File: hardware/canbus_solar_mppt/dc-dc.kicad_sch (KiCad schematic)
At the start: 58 parts

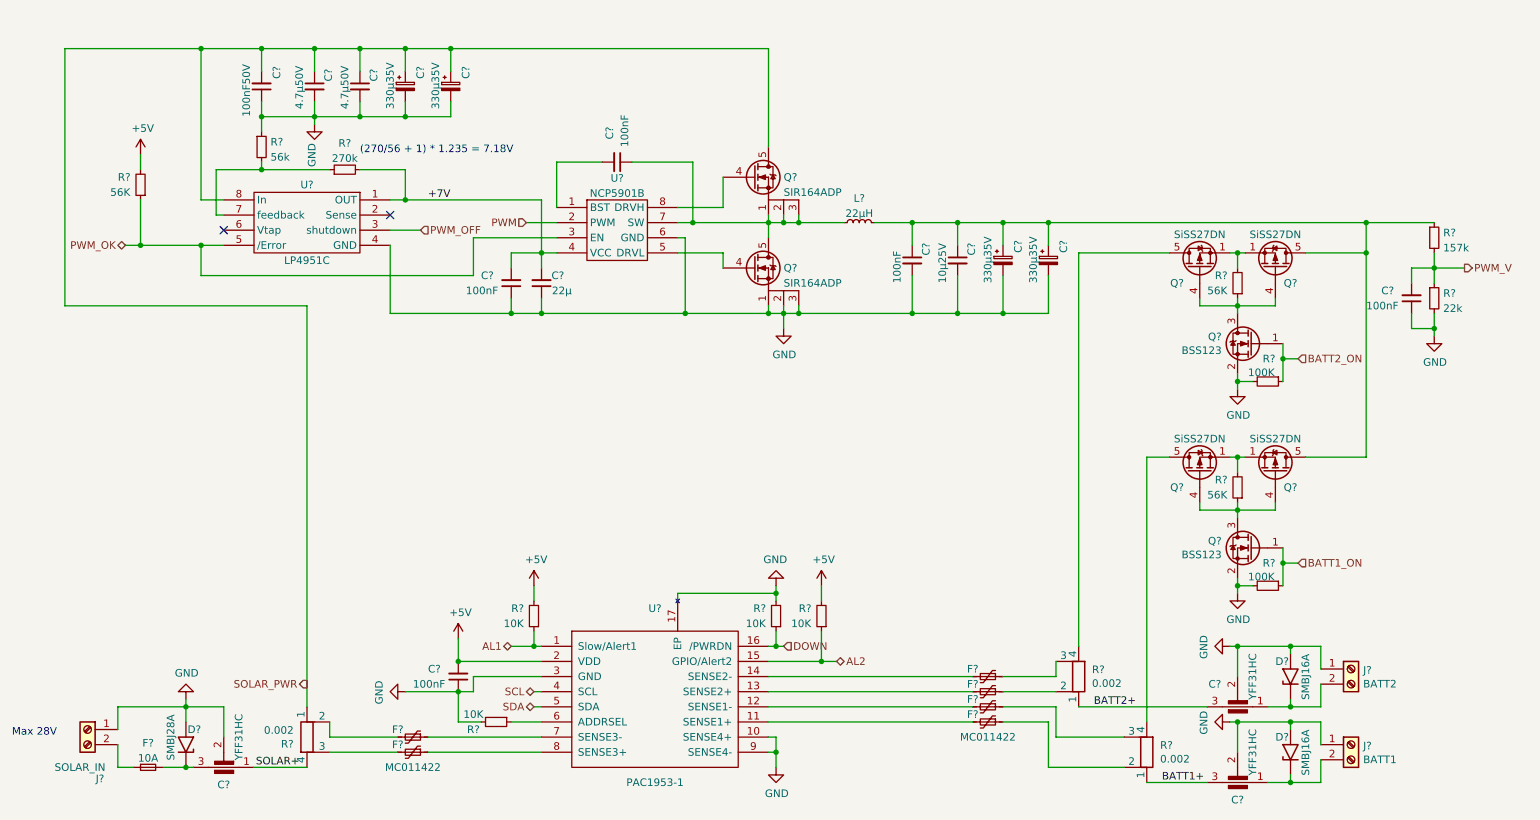
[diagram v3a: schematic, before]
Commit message: Add more signals between pic18 and DC/DC
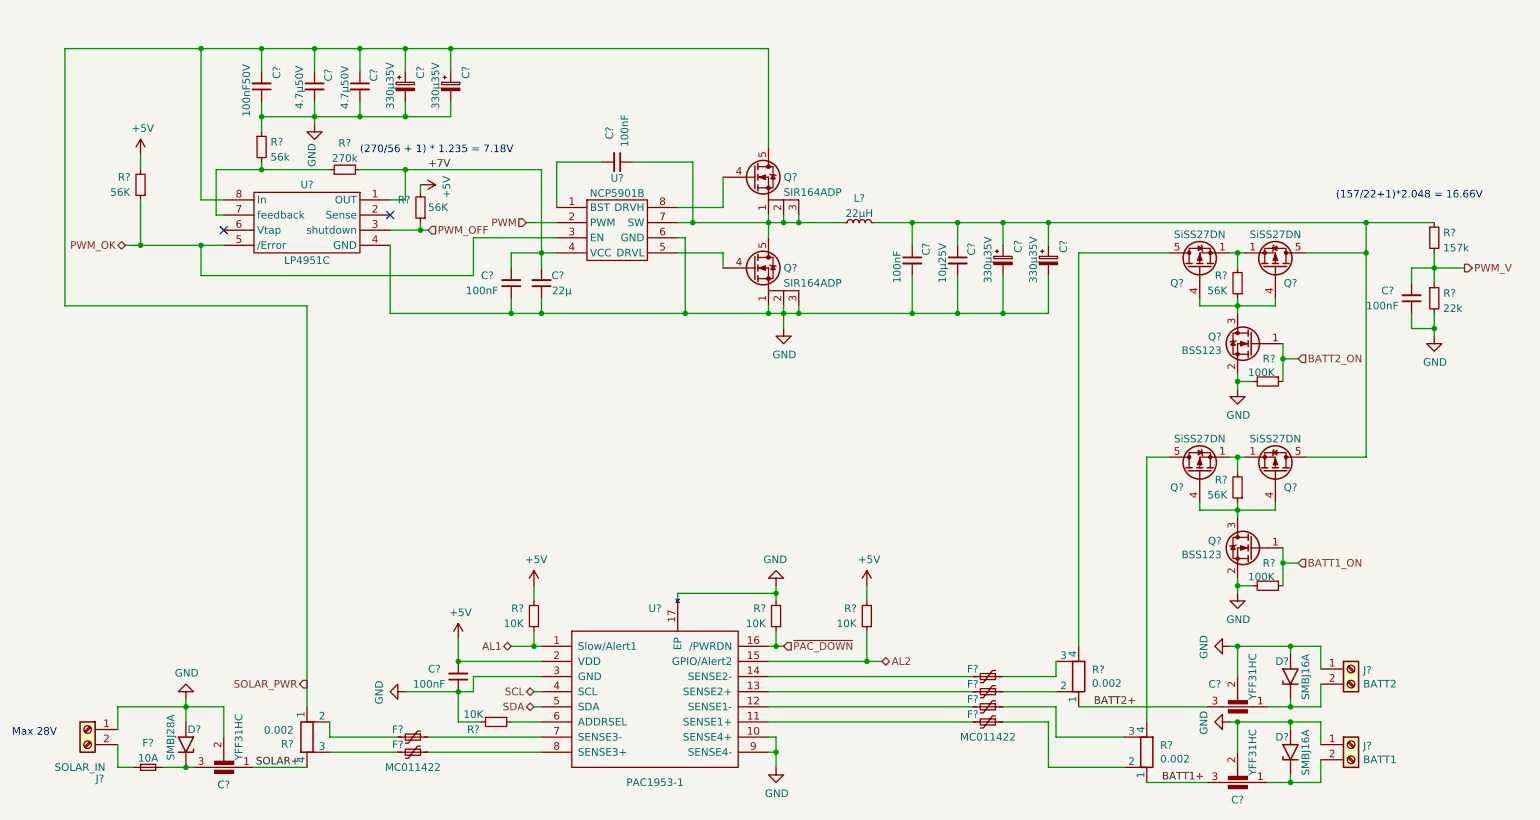
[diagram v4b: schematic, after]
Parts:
- added R?: 56K, Resistor_THT:R_Axial_DIN0207_L6.3mm_D2.5mm_P7.62mm_Horizontal, symbol Device:R_Small
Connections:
- net +5V: now also R?.2
- net PWM_OFF: now also R?.1
- net DOWN renamed ~{PAC_DOWN}
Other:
- note added: "(157/22+1)*2.048 = 16.66V"
- moved on the sheet: R?
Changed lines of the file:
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@@
   (junction (at 204.47 58.42) (diameter 0) (color 0 0 0 0)
   )
+  (junction (at 99.06 59.69) (diameter 0) (color 0 0 0 0)
+  )
   (junction (at 119.38 63.5) (diameter 0) (color 0 0 0 0)
   )
-  (junction (at 96.52 54.61) (diameter 0) (color 0 0 0 0)
-  )
   (junction (at 72.39 40.64) (diameter 0) (color 0 0 0 0)
   )
@@
   (junction (at 52.07 62.23) (diameter 0) (color 0 0 0 0)
   )
+  (junction (at 96.52 49.53) (diameter 0) (color 0 0 0 0)
+  )
   (junction (at 257.81 63.5) (diameter 0) (color 0 0 0 0)
   )
@@
   (junction (at 62.23 62.23) (diameter 0) (color 0 0 0 0)
   )
-  (junction (at 166.37 132.08) (diameter 0) (color 0 0 0 0)
+  (junction (at 173.99 132.08) (diameter 0) (color 0 0 0 0)
   )
   (junction (at 181.61 73.66) (diameter 0) (color 0 0 0 0)
@@
     (stroke (width 0) (type default) (color 0 0 0 0))
   )
+  (wire (pts (xy 119.38 49.53) (xy 119.38 63.5))
+    (stroke (width 0) (type default) (color 0 0 0 0))
+  )
   (wire (pts (xy 62.23 29.21) (xy 62.23 54.61))
     (stroke (width 0) (type default) (color 0 0 0 0))
@@
     (stroke (width 0) (type default) (color 0 0 0 0))
   )
-  (wire (pts (xy 157.48 132.08) (xy 166.37 132.08))
+  (wire (pts (xy 157.48 132.08) (xy 173.99 132.08))
     (stroke (width 0) (type default) (color 0 0 0 0))
   )
@@
     (stroke (width 0) (type default) (color 0 0 0 0))
   )
-  (wire (pts (xy 119.38 54.61) (xy 119.38 63.5))
-    (stroke (width 0) (type default) (color 0 0 0 0))
-  )
   (wire (pts (xy 96.52 40.64) (xy 104.14 40.64))
     (stroke (width 0) (type default) (color 0 0 0 0))
   )
+  (wire (pts (xy 99.06 52.07) (xy 99.06 53.34))
+    (stroke (width 0) (type default) (color 0 0 0 0))
+  )
   (wire (pts (xy 142.24 55.88) (xy 149.86 55.88))
     (stroke (width 0) (type default) (color 0 0 0 0))
@@
     (stroke (width 0) (type default) (color 0 0 0 0))
   )
-  (wire (pts (xy 166.37 132.08) (xy 166.37 127))
+  (wire (pts (xy 173.99 132.08) (xy 173.99 127))
     (stroke (width 0) (type default) (color 0 0 0 0))
   )
@@
     (stroke (width 0) (type default) (color 0 0 0 0))
   )
-  (wire (pts (xy 166.37 132.08) (xy 168.91 132.08))
+  (wire (pts (xy 173.99 132.08) (xy 176.53 132.08))
     (stroke (width 0) (type default) (color 0 0 0 0))
   )
@@
     (stroke (width 0) (type default) (color 0 0 0 0))
   )
+  (wire (pts (xy 96.52 49.53) (xy 119.38 49.53))
+    (stroke (width 0) (type default) (color 0 0 0 0))
+  )
   (wire (pts (xy 234.95 97.79) (xy 236.22 97.79))
     (stroke (width 0) (type default) (color 0 0 0 0))
@@
     (stroke (width 0) (type default) (color 0 0 0 0))
   )
-  (wire (pts (xy 96.52 54.61) (xy 119.38 54.61))
-    (stroke (width 0) (type default) (color 0 0 0 0))
-  )
   (wire (pts (xy 269.24 66.04) (xy 269.24 68.58))
     (stroke (width 0) (type default) (color 0 0 0 0))
@@
     (stroke (width 0) (type default) (color 0 0 0 0))
   )
+  (wire (pts (xy 99.06 58.42) (xy 99.06 59.69))
+    (stroke (width 0) (type default) (color 0 0 0 0))
+  )
   (wire (pts (xy 114.3 71.12) (xy 114.3 73.66))
     (stroke (width 0) (type default) (color 0 0 0 0))
@@
     (stroke (width 0) (type default) (color 0 0 0 0))
   )
-  (wire (pts (xy 166.37 121.92) (xy 166.37 119.38))
+  (wire (pts (xy 173.99 121.92) (xy 173.99 119.38))
     (stroke (width 0) (type default) (color 0 0 0 0))
   )
@@
   )
   (wire (pts (xy 236.22 97.79) (xy 236.22 100.33))
+    (stroke (width 0) (type default) (color 0 0 0 0))
+  )
+  (wire (pts (xy 99.06 59.69) (xy 100.33 59.69))
     (stroke (width 0) (type default) (color 0 0 0 0))
   )
@@
     (effects (font (size 1.27 1.27)) (justify left bottom))
   )
+  (text "(157/22+1)*2.048 = 16.66V" (at 252.73 54.61 0)
+    (effects (font (size 1.27 1.27)) (justify left bottom))
+  )
   (text "(270/56 + 1) * 1.235 = 7.18V" (at 88.9 46.99 0)
     (effects (font (size 1.27 1.27)) (justify left bottom))
   )
-  (label "+7V" (at 100.33 54.61 0)
+  (label "+7V" (at 100.33 49.53 0)
     (effects (font (size 1.27 1.27)) (justify left bottom))
   )
@@
     (effects (font (size 1.27 1.27)) (justify right))
   )
-  (hierarchical_label "PWM_OFF" (shape input) (at 99.06 59.69 0)
+  (hierarchical_label "PWM_OFF" (shape input) (at 100.33 59.69 0)
     (effects (font (size 1.27 1.27)) (justify left))
   )
@@
     (effects (font (size 1.27 1.27)) (justify right))
   )
-  (hierarchical_label "AL2" (shape bidirectional) (at 168.91 132.08 0)
+  (hierarchical_label "AL2" (shape bidirectional) (at 176.53 132.08 0)
     (effects (font (size 1.27 1.27)) (justify left))
   )
@@
     (effects (font (size 1.27 1.27)) (justify right))
   )
-  (hierarchical_label "DOWN" (shape input) (at 160.02 129.54 0)
+  (hierarchical_label "~{PAC_DOWN}" (shape input) (at 160.02 129.54 0)
     (effects (font (size 1.27 1.27)) (justify left))
   )
@@
     (pin "1")
     (pin "2")
+  )
+  (symbol (lib_id "power:+5V") (at 99.06 52.07 270) (unit 1)
+    (in_bom yes) (on_board yes)
+    (property "Reference" "#PWR?" (id 0) (at 95.25 52.07 0)
+      (effects (font (size 1.27 1.27)) hide)
+    )
+    (property "Value" "+5V" (id 1) (at 103.4542 52.451 0))
+    (property "Footprint" "" (id 2) (at 99.06 52.07 0)
+      (effects (font (size 1.27 1.27)) hide)
+    )
+    (property "Datasheet" "" (id 3) (at 99.06 52.07 0)
+      (effects (font (size 1.27 1.27)) hide)
+    )
+    (pin "1")
   )
   (symbol (lib_id "Device:C_Small") (at 189.23 64.77 0) (unit 1)
@@
     (pin "2")
   )
-  (symbol (lib_id "power:+5V") (at 166.37 119.38 0) (unit 1)
-    (in_bom yes) (on_board yes)
-    (property "Reference" "#PWR?" (id 0) (at 166.37 123.19 0)
-      (effects (font (size 1.27 1.27)) hide)
-    )
-    (property "Value" "+5V" (id 1) (at 166.751 114.9858 0))
-    (property "Footprint" "" (id 2) (at 166.37 119.38 0)
-      (effects (font (size 1.27 1.27)) hide)
-    )
-    (property "Datasheet" "" (id 3) (at 166.37 119.38 0)
+  (symbol (lib_id "power:+5V") (at 173.99 119.38 0) (unit 1)
+    (in_bom yes) (on_board yes)
+    (property "Reference" "#PWR?" (id 0) (at 173.99 123.19 0)
+      (effects (font (size 1.27 1.27)) hide)
+    )
+    (property "Value" "+5V" (id 1) (at 174.371 114.9858 0))
+    (property "Footprint" "" (id 2) (at 173.99 119.38 0)
+      (effects (font (size 1.27 1.27)) hide)
+    )
+    (property "Datasheet" "" (id 3) (at 173.99 119.38 0)
       (effects (font (size 1.27 1.27)) hide)
     )
@@
     (pin "2")
   )
-  (symbol (lib_id "Device:R_Small") (at 166.37 124.46 180) (unit 1)
-    (in_bom yes) (on_board yes)
-    (property "Reference" "R?" (id 0) (at 162.56 123.19 0)
-      (effects (font (size 1.27 1.27)) (justify right))
-    )
-    (property "Value" "10K" (id 1) (at 161.29 125.73 0)
-      (effects (font (size 1.27 1.27)) (justify right))
-    )
-    (property "Footprint" "Resistor_THT:R_Axial_DIN0207_L6.3mm_D2.5mm_P7.62mm_Horizontal" (id 2) (at 166.37 124.46 0)
-      (effects (font (size 1.27 1.27)) hide)
-    )
-    (property "Datasheet" "~" (id 3) (at 166.37 124.46 0)
+  (symbol (lib_id "Device:R_Small") (at 173.99 124.46 180) (unit 1)
+    (in_bom yes) (on_board yes)
+    (property "Reference" "R?" (id 0) (at 170.18 123.19 0)
+      (effects (font (size 1.27 1.27)) (justify right))
+    )
+    (property "Value" "10K" (id 1) (at 168.91 125.73 0)
+      (effects (font (size 1.27 1.27)) (justify right))
+    )
+    (property "Footprint" "Resistor_THT:R_Axial_DIN0207_L6.3mm_D2.5mm_P7.62mm_Horizontal" (id 2) (at 173.99 124.46 0)
+      (effects (font (size 1.27 1.27)) hide)
+    )
+    (property "Datasheet" "~" (id 3) (at 173.99 124.46 0)
       (effects (font (size 1.27 1.27)) hide)
     )
@@
       (effects (font (size 1.27 1.27)) hide)
     )
+    (pin "1")
+    (pin "2")
+  )
+  (symbol (lib_id "Device:R_Small") (at 99.06 55.88 180) (unit 1)
+    (in_bom yes) (on_board yes)
+    (property "Reference" "R?" (id 0) (at 95.25 54.61 0)
+      (effects (font (size 1.27 1.27)) (justify right))
+    )
+    (property "Value" "56K" (id 1) (at 100.33 55.88 0)
+      (effects (font (size 1.27 1.27)) (justify right))
+    )
+    (property "Footprint" "Resistor_THT:R_Axial_DIN0207_L6.3mm_D2.5mm_P7.62mm_Horizontal" (id 2) (at 99.06 55.88 0)
+      (effects (font (size 1.27 1.27)) hide)
+    )
+    (property "Datasheet" "~" (id 3) (at 99.06 55.88 0)
+      (effects (font (size 1.27 1.27)) hide)
+    )

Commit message: Add footprint for OLED display annotate schematic run and fix ERC
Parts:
- gave numbers to parts that had none: 59

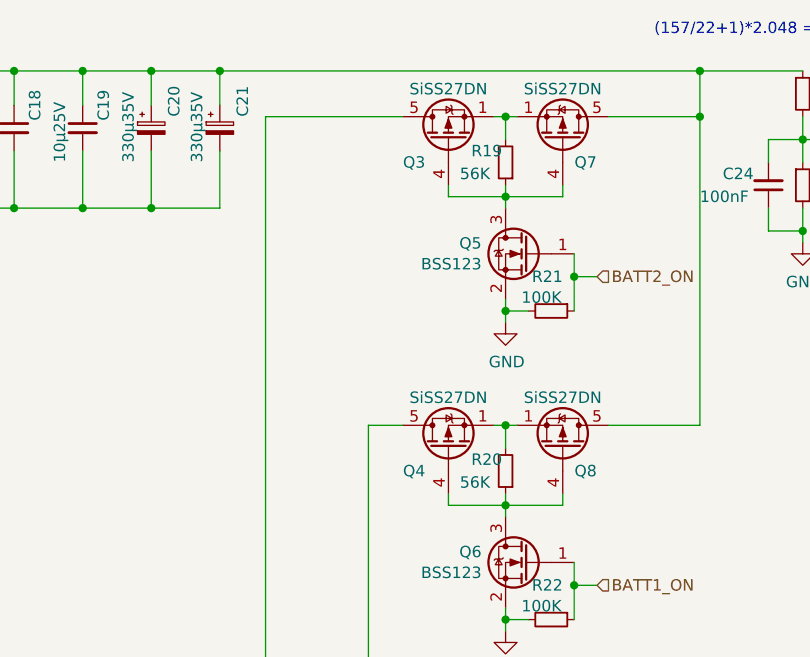
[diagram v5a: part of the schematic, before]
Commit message: Decrease pull gate resitors of P-MOS to decrease turn-off time. Maybe switch to a gate driver ic ?
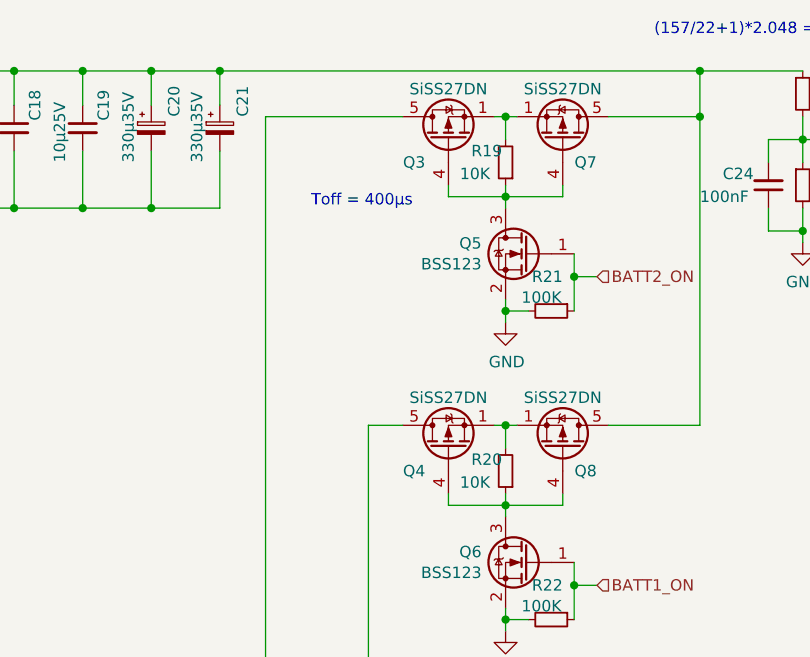
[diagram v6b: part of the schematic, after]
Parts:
- R19, R20: value 56K -> 10K
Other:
- note added: "Toff = 400µs"
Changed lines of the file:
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@@
+    (effects (font (size 1.27 1.27)) (justify left bottom))
+  )
+  (text "Toff = 400µs" (at 214.63 73.66 0)
     (effects (font (size 1.27 1.27)) (justify left bottom))
   )
@@
       (effects (font (size 1.27 1.27)) (justify right))
     )
-    (property "Value" "56K" (id 1) (at 231.14 69.85 0)
+    (property "Value" "10K" (id 1) (at 231.14 69.85 0)
       (effects (font (size 1.27 1.27)) (justify right))
     )
@@
       (effects (font (size 1.27 1.27)) (justify right))
     )
-    (property "Value" "56K" (id 1) (at 231.14 104.14 0)
-      (effects (font (size 1.27 1.27)) (justify right))
-    )
+    (property "Value" "10K" (id 1) (at 231.14 104.14 0)
+      (effects (font (size 1.27 1.27)) (justify right))
+    )

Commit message: Fix up resistor footprints, use only SMD for now.
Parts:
- R12, R8: footprint Resistor_THT:R_Axial_DIN0207_L6.3mm_D2.5mm_P7.62mm_Horizontal -> Resistor_SMD:R_1206_3216Metric_Pad1.30x1.75mm_HandSolder
- R13, R14, R16, R19, R20, R21, R22: footprint Resistor_THT:R_Axial_DIN0207_L6.3mm_D2.5mm_P7.62mm_Horizontal -> Resistor_SMD:R_0805_2012Metric_Pad1.20x1.40mm_HandSolder
- R15: footprint Resistor_SMD:R_1206_3216Metric_Pad1.30x1.75mm_HandSolder -> Resistor_SMD:R_0805_2012Metric_Pad1.20x1.40mm_HandSolder
- R9: footprint Resistor_SMD:R_0805_2012Metric_Pad1.20x1.40mm_HandSolder -> Resistor_SMD:R_1206_3216Metric_Pad1.30x1.75mm_HandSolder
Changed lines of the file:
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@@
       (effects (font (size 1.27 1.27)) (justify right))
     )
-    (property "Footprint" "Resistor_THT:R_Axial_DIN0207_L6.3mm_D2.5mm_P7.62mm_Horizontal" (id 2) (at 118.11 124.46 0)
+    (property "Footprint" "Resistor_SMD:R_0805_2012Metric_Pad1.20x1.40mm_HandSolder" (id 2) (at 118.11 124.46 0)
       (effects (font (size 1.27 1.27)) hide)
     )
@@
       (effects (font (size 1.27 1.27)) (justify right))
     )
-    (property "Footprint" "Resistor_THT:R_Axial_DIN0207_L6.3mm_D2.5mm_P7.62mm_Horizontal" (id 2) (at 236.22 68.58 0)
+    (property "Footprint" "Resistor_SMD:R_0805_2012Metric_Pad1.20x1.40mm_HandSolder" (id 2) (at 236.22 68.58 0)
       (effects (font (size 1.27 1.27)) hide)
     )
@@
       (effects (font (size 1.27 1.27)) (justify right))
     )
-    (property "Footprint" "Resistor_THT:R_Axial_DIN0207_L6.3mm_D2.5mm_P7.62mm_Horizontal" (id 2) (at 241.3 85.09 0)
+    (property "Footprint" "Resistor_SMD:R_0805_2012Metric_Pad1.20x1.40mm_HandSolder" (id 2) (at 241.3 85.09 0)
       (effects (font (size 1.27 1.27)) hide)
     )
@@
       (effects (font (size 1.27 1.27)) (justify right))
     )
-    (property "Footprint" "Resistor_SMD:R_1206_3216Metric_Pad1.30x1.75mm_HandSolder" (id 2) (at 158.75 124.46 0)
+    (property "Footprint" "Resistor_SMD:R_0805_2012Metric_Pad1.20x1.40mm_HandSolder" (id 2) (at 158.75 124.46 0)
       (effects (font (size 1.27 1.27)) hide)
     )
@@
       (effects (font (size 1.27 1.27)) (justify right))
     )
-    (property "Footprint" "Resistor_THT:R_Axial_DIN0207_L6.3mm_D2.5mm_P7.62mm_Horizontal" (id 2) (at 173.99 124.46 0)
+    (property "Footprint" "Resistor_SMD:R_0805_2012Metric_Pad1.20x1.40mm_HandSolder" (id 2) (at 173.99 124.46 0)
       (effects (font (size 1.27 1.27)) hide)
     )
@@
       (effects (font (size 1.27 1.27)) (justify right))
     )
-    (property "Footprint" "Resistor_THT:R_Axial_DIN0207_L6.3mm_D2.5mm_P7.62mm_Horizontal" (id 2) (at 52.07 52.07 0)
+    (property "Footprint" "Resistor_SMD:R_1206_3216Metric_Pad1.30x1.75mm_HandSolder" (id 2) (at 52.07 52.07 0)
       (effects (font (size 1.27 1.27)) hide)
     )
@@
       (effects (font (size 1.27 1.27)) (justify right))
     )
-    (property "Footprint" "Resistor_THT:R_Axial_DIN0207_L6.3mm_D2.5mm_P7.62mm_Horizontal" (id 2) (at 236.22 102.87 0)
+    (property "Footprint" "Resistor_SMD:R_0805_2012Metric_Pad1.20x1.40mm_HandSolder" (id 2) (at 236.22 102.87 0)
       (effects (font (size 1.27 1.27)) hide)
     )
@@
       (effects (font (size 1.27 1.27)) (justify right))
     )
-    (property "Footprint" "Resistor_THT:R_Axial_DIN0207_L6.3mm_D2.5mm_P7.62mm_Horizontal" (id 2) (at 99.06 55.88 0)
+    (property "Footprint" "Resistor_SMD:R_1206_3216Metric_Pad1.30x1.75mm_HandSolder" (id 2) (at 99.06 55.88 0)
       (effects (font (size 1.27 1.27)) hide)
     )
@@
       (effects (font (size 1.27 1.27)) (justify left))
     )
-    (property "Footprint" "Resistor_SMD:R_0805_2012Metric_Pad1.20x1.40mm_HandSolder" (id 2) (at 72.39 45.72 0)
+    (property "Footprint" "Resistor_SMD:R_1206_3216Metric_Pad1.30x1.75mm_HandSolder" (id 2) (at 72.39 45.72 0)
       (effects (font (size 1.27 1.27)) hide)
     )
@@
     (property "Reference" "R13" (id 0) (at 107.95 143.51 90))
     (property "Value" "10K" (id 1) (at 107.95 140.97 90))
-    (property "Footprint" "Resistor_THT:R_Axial_DIN0207_L6.3mm_D2.5mm_P7.62mm_Horizontal" (id 2) (at 111.76 142.24 0)
+    (property "Footprint" "Resistor_SMD:R_0805_2012Metric_Pad1.20x1.40mm_HandSolder" (id 2) (at 111.76 142.24 0)
       (effects (font (size 1.27 1.27)) hide)
     )
@@
       (effects (font (size 1.27 1.27)) (justify right))
     )
-    (property "Footprint" "Resistor_THT:R_Axial_DIN0207_L6.3mm_D2.5mm_P7.62mm_Horizontal" (id 2) (at 241.3 119.38 0)
-      (effects (font (size 1.27 1.27)) hide)
-    )
+    (property "Footprint" "Resistor_SMD:R_0805_2012Metric_Pad1.20x1.40mm_HandSolder" (id 2) (at 241.3 119.38 0)
+      (effects (font (size 1.27 1.27)) hide)
+    )
